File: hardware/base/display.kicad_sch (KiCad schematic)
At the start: 3 parts, among them J5 Conn_02x15_Odd_Even_MountingP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

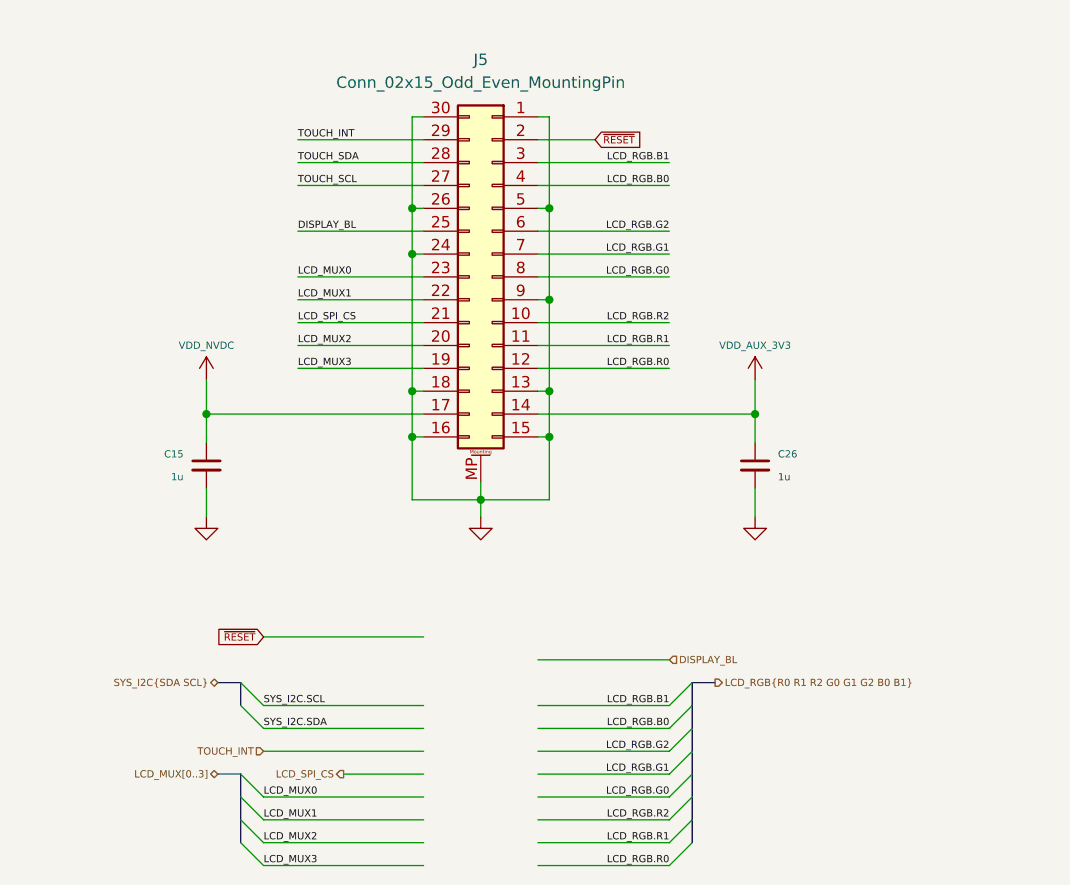
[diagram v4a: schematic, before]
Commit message: screen design freeze, 3d model added to base, routed display connector, sd, usb
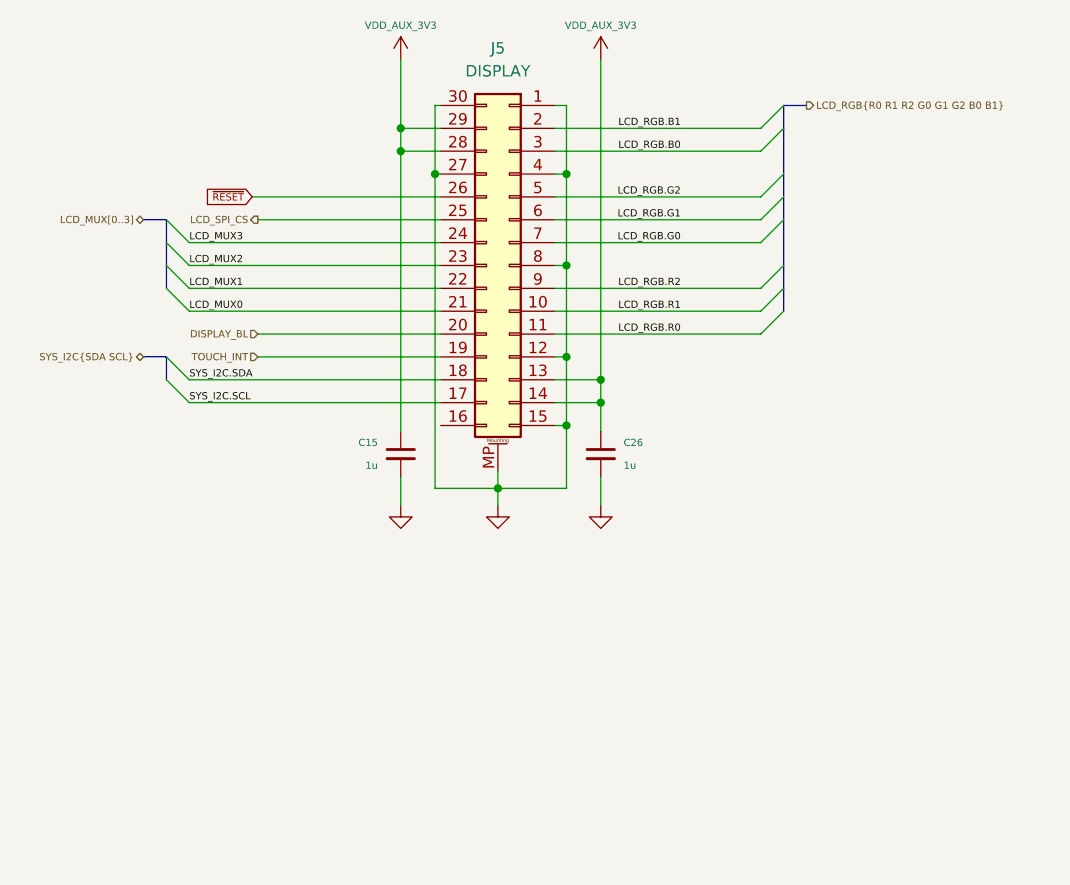
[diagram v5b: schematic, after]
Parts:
- J5: value Conn_02x15_Odd_Even_MountingPin -> DISPLAY
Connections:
- net TOUCH_SCL is gone; now on net GND: J5.27 (Pin_27)
- net TOUCH_SDA is gone; now on net VDD_AUX_3V3: J5.28 (Pin_28)
- net DISPLAY_BL: now also J5.20 (Pin_20); no longer J5.25 (Pin_25)
- net GND: now also J5.12 (Pin_12), J5.4 (Pin_4), J5.8 (Pin_8); no longer J5.13 (Pin_13), J5.16 (Pin_16), J5.18 (Pin_18), J5.24 (Pin_24), J5.26 (Pin_26), J5.5 (Pin_5), J5.9 (Pin_9)
- net LCD_MUX0: now also J5.21 (Pin_21); no longer J5.23 (Pin_23)
- net LCD_MUX2: now also J5.23 (Pin_23); no longer J5.20 (Pin_20)
- net LCD_MUX3: now also J5.24 (Pin_24); no longer J5.19 (Pin_19)
- net LCD_RGB.B0: now also J5.3 (Pin_3); no longer J5.4 (Pin_4)
- net LCD_RGB.B1: now also J5.2 (Pin_2); no longer J5.3 (Pin_3)
- net LCD_RGB.G0: now also J5.7 (Pin_7); no longer J5.8 (Pin_8)
- net LCD_RGB.G1: now also J5.6 (Pin_6); no longer J5.7 (Pin_7)
- net LCD_RGB.G2: now also J5.5 (Pin_5); no longer J5.6 (Pin_6)
- net LCD_RGB.R0: now also J5.11 (Pin_11); no longer J5.12 (Pin_12)
- net LCD_RGB.R1: now also J5.10 (Pin_10); no longer J5.11 (Pin_11)
- net LCD_RGB.R2: now also J5.9 (Pin_9); no longer J5.10 (Pin_10)
- net LCD_SPI_CS: now also J5.25 (Pin_25); no longer J5.21 (Pin_21)
- net SYS_I2C.SCL: now also J5.17 (Pin_17)
- net SYS_I2C.SDA: now also J5.18 (Pin_18)
- net TOUCH_INT: now also J5.19 (Pin_19); no longer J5.29 (Pin_29)
- net VDD_AUX_3V3: now also C15.1, J5.13 (Pin_13), J5.29 (Pin_29)
- net ~{RESET}: now also J5.26 (Pin_26); no longer J5.2 (Pin_2)
- removed net VDD_NVDC: C15.1, J5.17 (Pin_17)
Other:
- moved on the sheet: J5

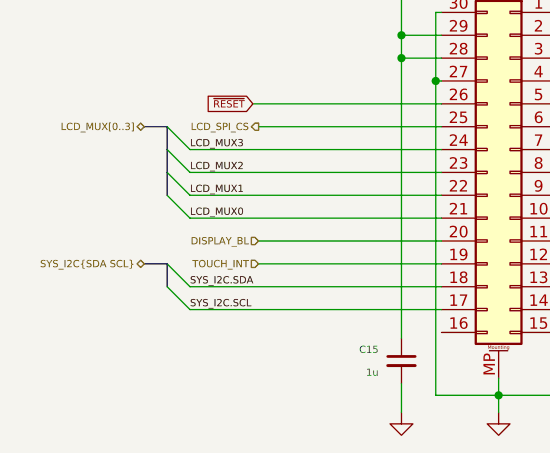
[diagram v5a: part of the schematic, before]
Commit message: layout complete, drc checks and tweaks to silkscreen, attempting geo reannotate
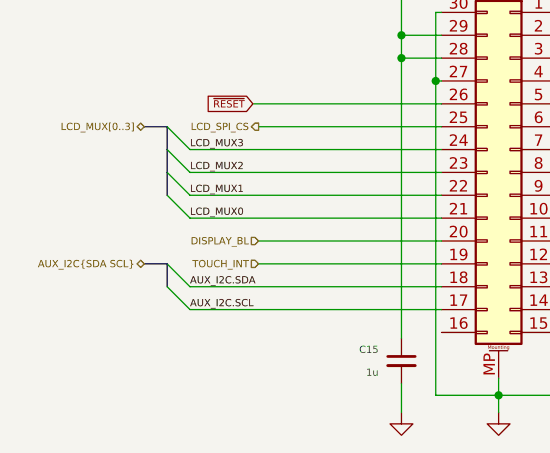
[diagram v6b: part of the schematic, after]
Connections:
- net SYS_I2C.SCL renamed AUX_I2C.SCL
- net SYS_I2C.SDA renamed AUX_I2C.SDA
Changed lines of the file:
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@@
     (effects (font (size 0.8 0.8)) (justify left bottom))
   )
-  (label "SYS_I2C.SCL" (at 71.12 91.44 0)
+  (label "AUX_I2C.SCL" (at 71.12 91.44 0)
     (effects (font (size 0.8 0.8)) (justify left bottom))
   )
@@
     (effects (font (size 0.8 0.8)) (justify left bottom))
   )
-  (label "SYS_I2C.SDA" (at 71.12 88.9 0)
+  (label "AUX_I2C.SDA" (at 71.12 88.9 0)
     (effects (font (size 0.8 0.8)) (justify left bottom))
   )
@@
     (effects (font (size 0.8 0.8)) (justify right))
   )
-  (hierarchical_label "SYS_I2C{SDA SCL}" (shape bidirectional) (at 66.04 86.36 180)
+  (hierarchical_label "AUX_I2C{SDA SCL}" (shape bidirectional) (at 66.04 86.36 180)
     (effects (font (size 0.8 0.8)) (justify right))
   )
